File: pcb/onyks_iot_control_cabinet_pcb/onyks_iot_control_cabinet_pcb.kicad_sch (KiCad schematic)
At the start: 20 parts, among them J4 Conn_01x02_Socket, Q3 SQ4940CEY-T1_GE3, SW1 SW_Push, SW2 SW_Push, SW3 SW_Push

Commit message: Fix the project; cleaning up the things
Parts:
- removed BZ?: Buzzer, symbol Device:Buzzer
- removed J4: Conn_01x02_Socket, symbol Connector:Conn_01x02_Socket
- removed Q3, Q?: SQ4940CEY-T1_GE3, symbol Simulation_SPICE:NMOS
- removed Q? (x2): NPN, symbol Simulation_SPICE:NPN
- removed R? (x2): 10k, symbol Device:R
- removed R?: 100, symbol Device:R
- removed U?: ESP32-WROOM-32D, RF_Module:ESP32-WROOM-32D, symbol RF_Module:ESP32-WROOM-32D
- added BZ1: Buzzer, symbol Device:Buzzer
- added J1: Conn_01x02_Socket, symbol Connector:Conn_01x02_Socket
- added Q1, Q2: SQ4940CEY-T1_GE3, symbol Simulation_SPICE:NMOS
- added Q3, Q4: NPN, symbol Simulation_SPICE:NPN
- added R2: 100, symbol Device:R
- added R3, R4: 10k, symbol Device:R
- added U1: ESP32-WROOM-32D, RF_Module:ESP32-WROOM-32D, symbol RF_Module:ESP32-WROOM-32D
- C1: value 0.1u -> 22u
- C4: value 22u -> 0.1u
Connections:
- net +12V: now also BZ1.1 (+)
- net +3.3V: now also C1.1, C2.1, J1.1 (Pin_1), U1.2 (VDD); no longer C3.1, C4.1
- net BUZZER_SWITCH: now also Q2.2 (G), R2.1, U1.26 (IO4)
- net DTR: now also Q3.3 (E), R4.2
- net FREE_GPIO_1: now also U1.24 (IO2)
- net FREE_GPIO_2: now also U1.29 (IO5)
- net FREE_GPIO_3: now also U1.27 (IO16)
- net FREE_GPIO_4: now also U1.28 (IO17)
- net FREE_GPIO_7: now also U1.7 (IO35)
- net GND: now also C1.2, C2.2, C3.1, C4.1, Q1.3 (S), Q2.3 (S), R2.2, U1.1 (GND), U1.15 (GND), U1.38 (GND), U1.39 (GND); no longer C1.1, C2.1, C3.2, C4.2
- net JTAG_MTCK: now also U1.16 (IO13)
- net JTAG_MTDI: now also U1.14 (IO12)
- net JTAG_MTDO: now also U1.23 (IO15)
- net JTAG_MTMS: now also U1.13 (IO14)
- net LOCK_MCU_MANUAL_OPEN: now also J1.2 (Pin_2), U1.31 (IO19)
- net LOCK_MINUS: now also Q1.1 (D)
- net LOCK_SWITCH: now also Q1.2 (G), U1.30 (IO18)
- net MCU_BOOT: now also C3.2, Q3.1 (C), U1.25 (IO0); no longer C1.2
- net MCU_RESET: now also C4.2, Q4.1 (C), U1.3 (EN); no longer C2.2
- net MCU_RX_PROG: now also U1.34 (RXD0/IO3)
- net MCU_TX_PROG: now also U1.35 (TXD0/IO1)
- net NFC_IRQ: now also U1.11 (IO26)
- net NFC_MISO: now also U1.10 (IO25)
- net NFC_MOSI: now also U1.37 (IO23)
- net NFC_RST: now also U1.12 (IO27)
- net RTS: now also Q4.3 (E), R3.2
- net at D1.4 (BK): now also U1.6 (IO34)
- net at D1.2 (RK): now also U1.8 (IO32)
- net at D1.3 (GK): now also U1.9 (IO33)
- new net: Q4.2 (B), R4.1
- new net: BZ1.2 (-), Q2.1 (D)
- new net: Q3.2 (B), R3.1
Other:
- removed sheet Connnectors
- removed sheet Power Supply and NFC Connector
- added sheet connnectors (connectors.kicad_sch)
- added sheet power_supply_nfc_connector (power_supply_nfc_connector.kicad_sch)
- title: Onyks IoT Control Cabinet -> Onyks Iot Control Cabinet

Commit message: Assignment some footprints to symbols
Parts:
- J1: footprint (none) -> Connector_PinHeader_2.54mm:PinHeader_1x02_P2.54mm_Vertical
- Q1, Q2: footprint (none) -> ourFootprints:QFN50P600X600X100-41N-D
- R1, R2, R3, R4: footprint (none) -> Resistor_SMD:R_0805_2012Metric_Pad1.20x1.40mm_HandSolder
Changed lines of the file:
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@@
 			)
 		)
-		(property "Footprint" ""
+		(property "Footprint" "Resistor_SMD:R_0805_2012Metric_Pad1.20x1.40mm_HandSolder"
 			(at 126.492 176.53 90)
 			(effects
@@
 			)
 		)
-		(property "Footprint" ""
+		(property "Footprint" "Resistor_SMD:R_0805_2012Metric_Pad1.20x1.40mm_HandSolder"
 			(at 138.43 56.388 90)
 			(effects
@@
 			)
 		)
-		(property "Footprint" ""
+		(property "Footprint" "ourFootprints:QFN50P600X600X100-41N-D"
 			(at 67.31 170.18 0)
 			(effects
@@
 			)
 		)
-		(property "Footprint" ""
+		(property "Footprint" "Resistor_SMD:R_0805_2012Metric_Pad1.20x1.40mm_HandSolder"
 			(at 138.43 76.708 90)
 			(effects
@@
 			)
 		)
-		(property "Footprint" ""
+		(property "Footprint" "Resistor_SMD:R_0805_2012Metric_Pad1.20x1.40mm_HandSolder"
 			(at 49.022 176.53 90)
 			(effects
@@
 			)
 		)
-		(property "Footprint" ""
+		(property "Footprint" "ourFootprints:QFN50P600X600X100-41N-D"
 			(at 144.78 170.18 0)
 			(effects
@@
 			)
 		)
-		(property "Footprint" ""
+		(property "Footprint" "Connector_PinHeader_2.54mm:PinHeader_1x02_P2.54mm_Vertical"
 			(at 237.49 72.39 0)
 			(effects

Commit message: PCB - Finished, needs additional confirmation
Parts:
- removed D1: LED_ARGB, symbol Device:LED_ARGB
- added D1: WS2812B, LED_SMD:LED_WS2812B_PLCC4_5.0x5.0mm_P3.2mm, symbol LED:WS2812B
- BZ1: footprint (none) -> ourFootprints:CPI2416100T
- C1, C2, C3, C4, C5: footprint (none) -> Capacitor_SMD:C_0805_2012Metric
- Q1, Q2: footprint ourFootprints:QFN50P600X600X100-41N-D -> ourFootprints:SOIC127P600X175-8N
- Q3, Q4: footprint (none) -> Package_TO_SOT_SMD:SOT-23-3
- SW1, SW2, SW3: footprint (none) -> Button_Switch_SMD:SW_Push_SPST_NO_Alps_SKRK
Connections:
- net +12V: now also BZ1.A1 (-_1), BZ1.B1 (+_1), BZ1.B2 (+_2); no longer BZ1.1 (+)
- net +3.3V: now also D1.1 (VDD)
- net BUZZER_SWITCH: now also Q2.4 (G); no longer Q2.2 (G)
- net FREE_GPIO_5: now also U1.33 (IO21)
- net FREE_GPIO_6: now also U1.36 (IO22)
- net FREE_GPIO_7: now also U1.9 (IO33); no longer U1.7 (IO35)
- net GND: now also Q1.1 (S), Q1.2 (S), Q2.1 (S), Q2.2 (S), D1.3 (VSS)
- net LOCK_MINUS: now also Q1.5 (D), Q1.6 (D), Q1.7 (D), Q1.8 (D); no longer Q1.1 (D)
- net LOCK_SWITCH: now also Q1.4 (G); no longer Q1.2 (G)
- net FREE_GPIO_8: now reaches U1.6 (IO34)
- net at U1.8 (IO32): now also D1.4 (DIN)
- new net: BZ1.A2 (-_2), Q2.5 (D), Q2.6 (D), Q2.7 (D), Q2.8 (D)
- new net FREE_GPIO_9: U1.7 (IO35)
- no-connect marks 8 -> 9
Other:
- sheet connnectors ports: added GPIO_8, GPIO_9; removed none

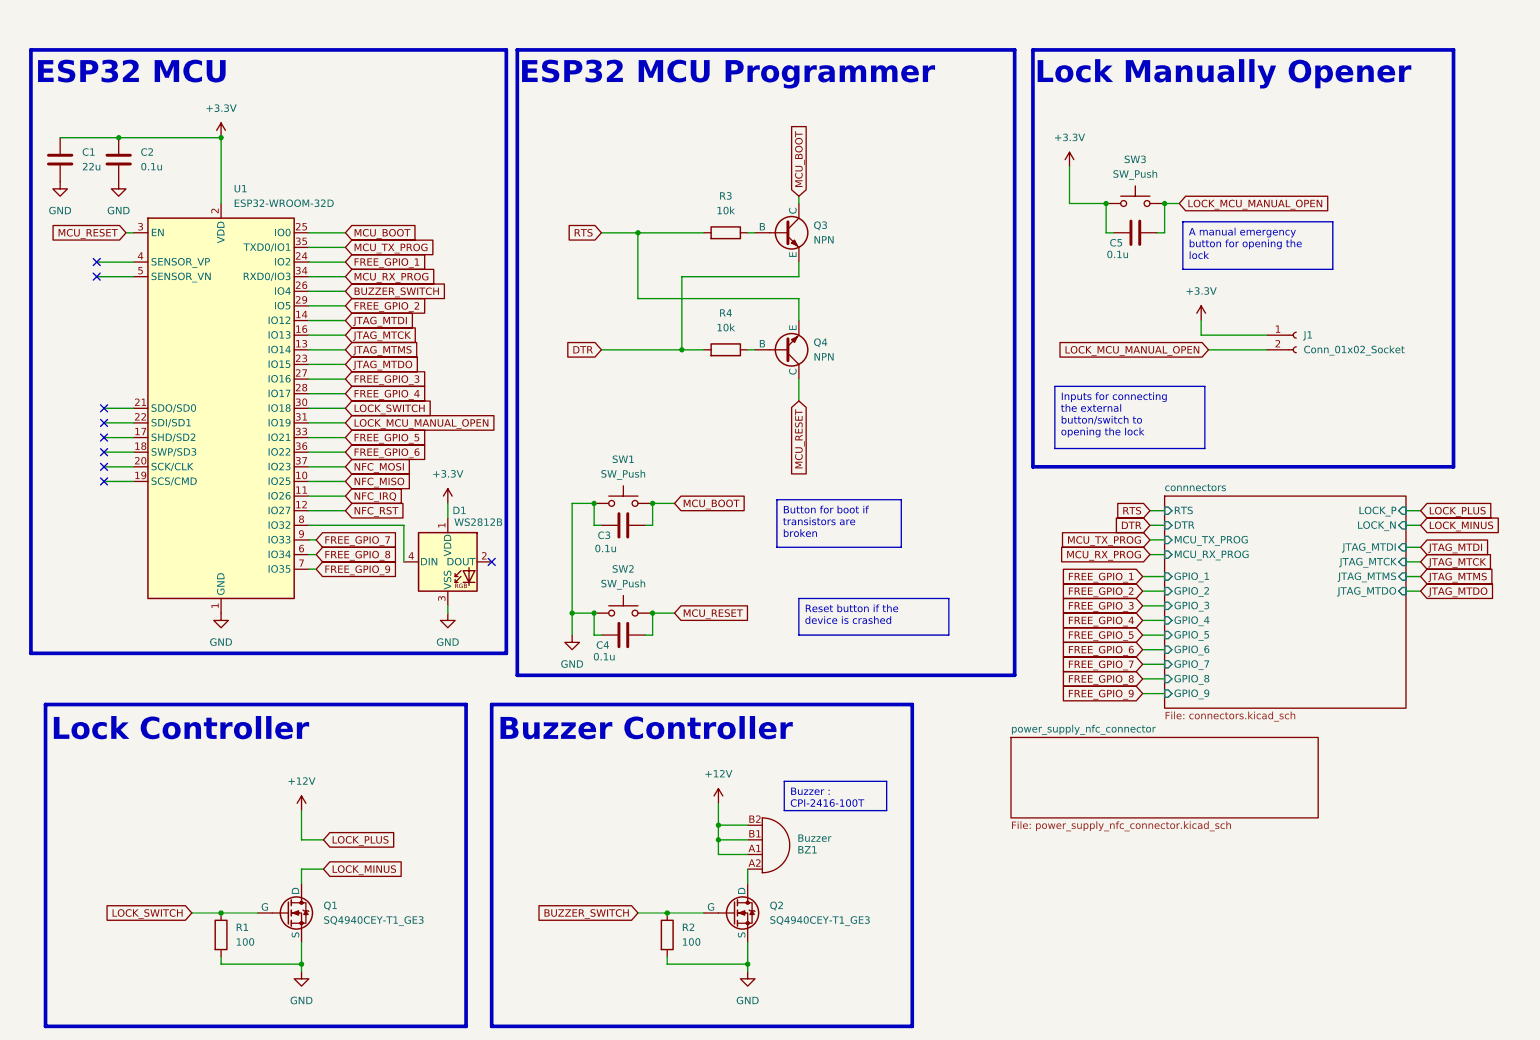
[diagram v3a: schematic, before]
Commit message: Change some elements footprints
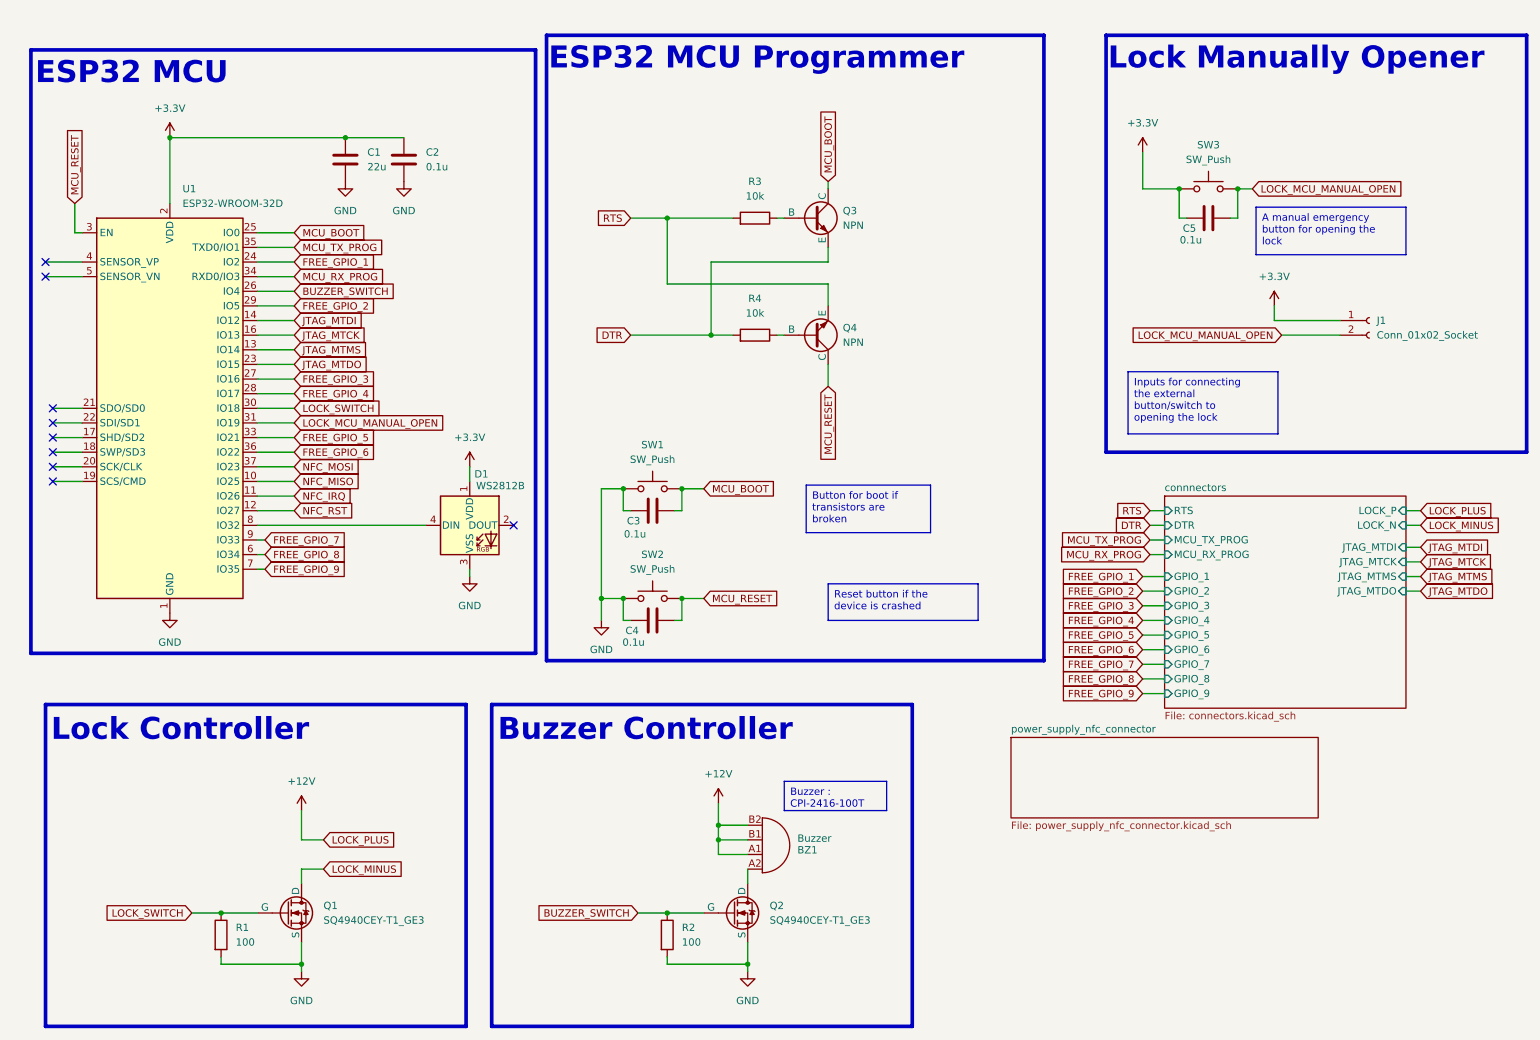
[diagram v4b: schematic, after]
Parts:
- SW1, SW2, SW3: footprint Button_Switch_SMD:SW_Push_SPST_NO_Alps_SKRK -> Button_Switch_SMD:SW_Tactile_SPST_NO_Straight_CK_PTS636Sx25SMTRLFS
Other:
- moved on the sheet: C1, C2, C3, C4, C5, D1, J1, Q3, Q4, R3, R4, SW1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

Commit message: Fixed minor mistakes (name of MOS component)
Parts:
- Q1, Q2: value SQ4940CEY-T1_GE3 -> SQ4050EY-T1_GE3
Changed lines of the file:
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@@
 			)
 		)
-		(property "Value" "SQ4940CEY-T1_GE3"
+		(property "Value" "SQ4050EY-T1_GE3"
 			(at 146.05 173.9899 0)
 			(effects
@@
 			)
 		)
-		(property "Value" "SQ4940CEY-T1_GE3"
+		(property "Value" "SQ4050EY-T1_GE3"
 			(at 68.58 173.9899 0)
 			(effects

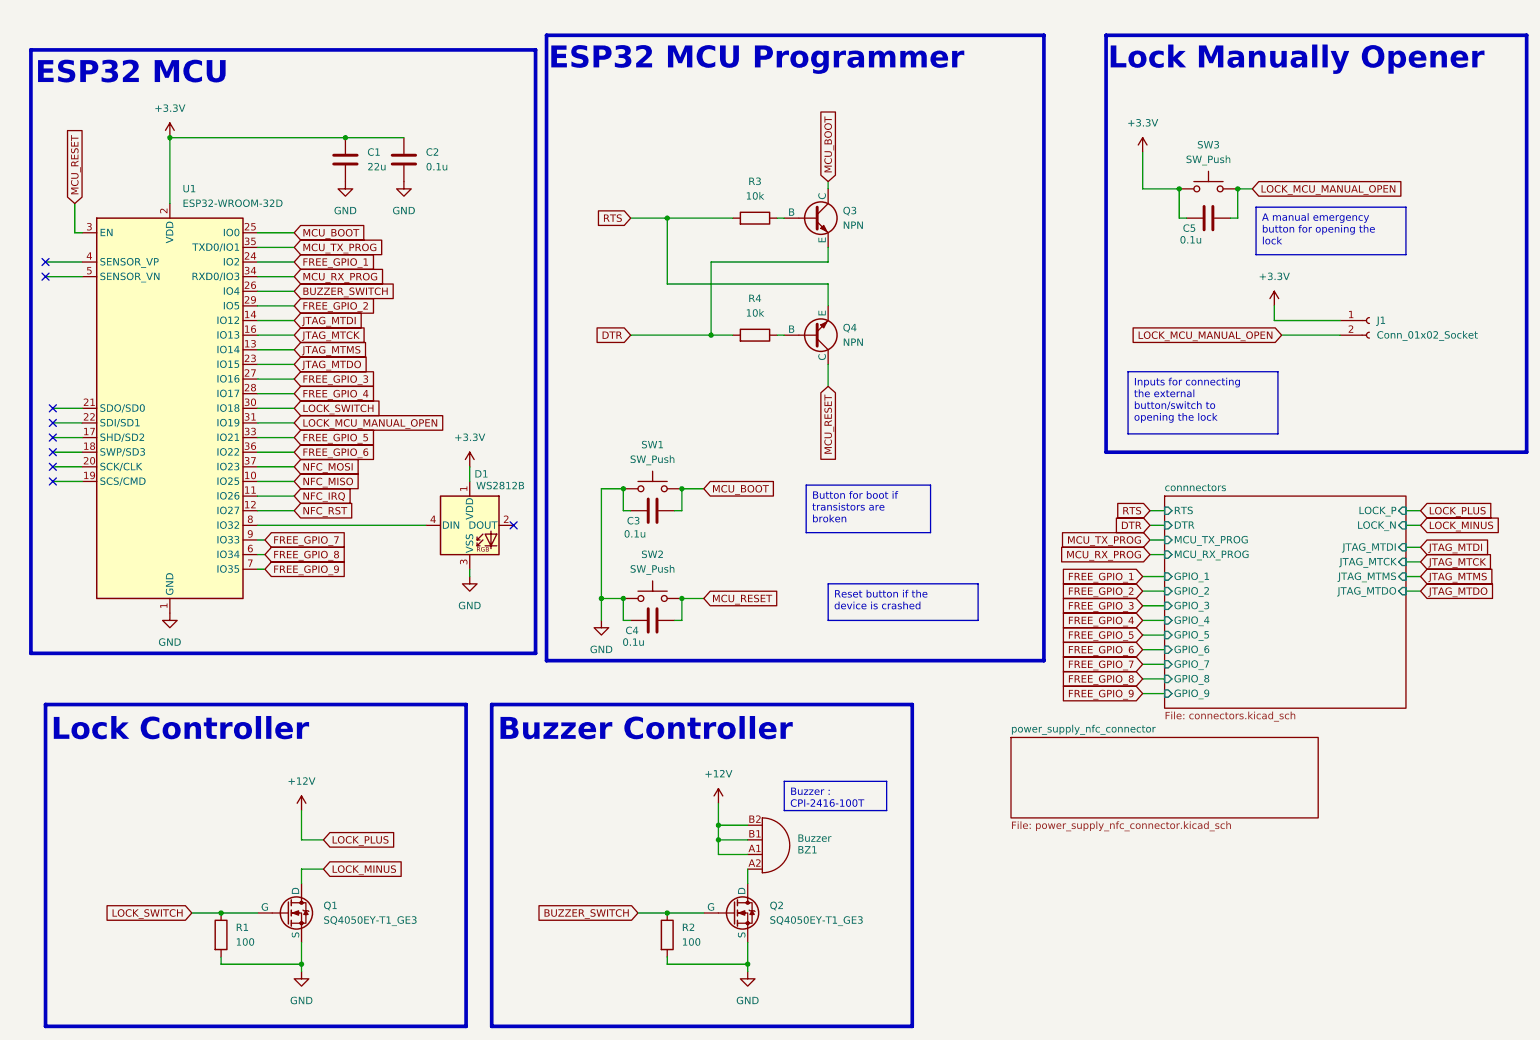
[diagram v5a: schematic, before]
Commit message: Redrawing schematics
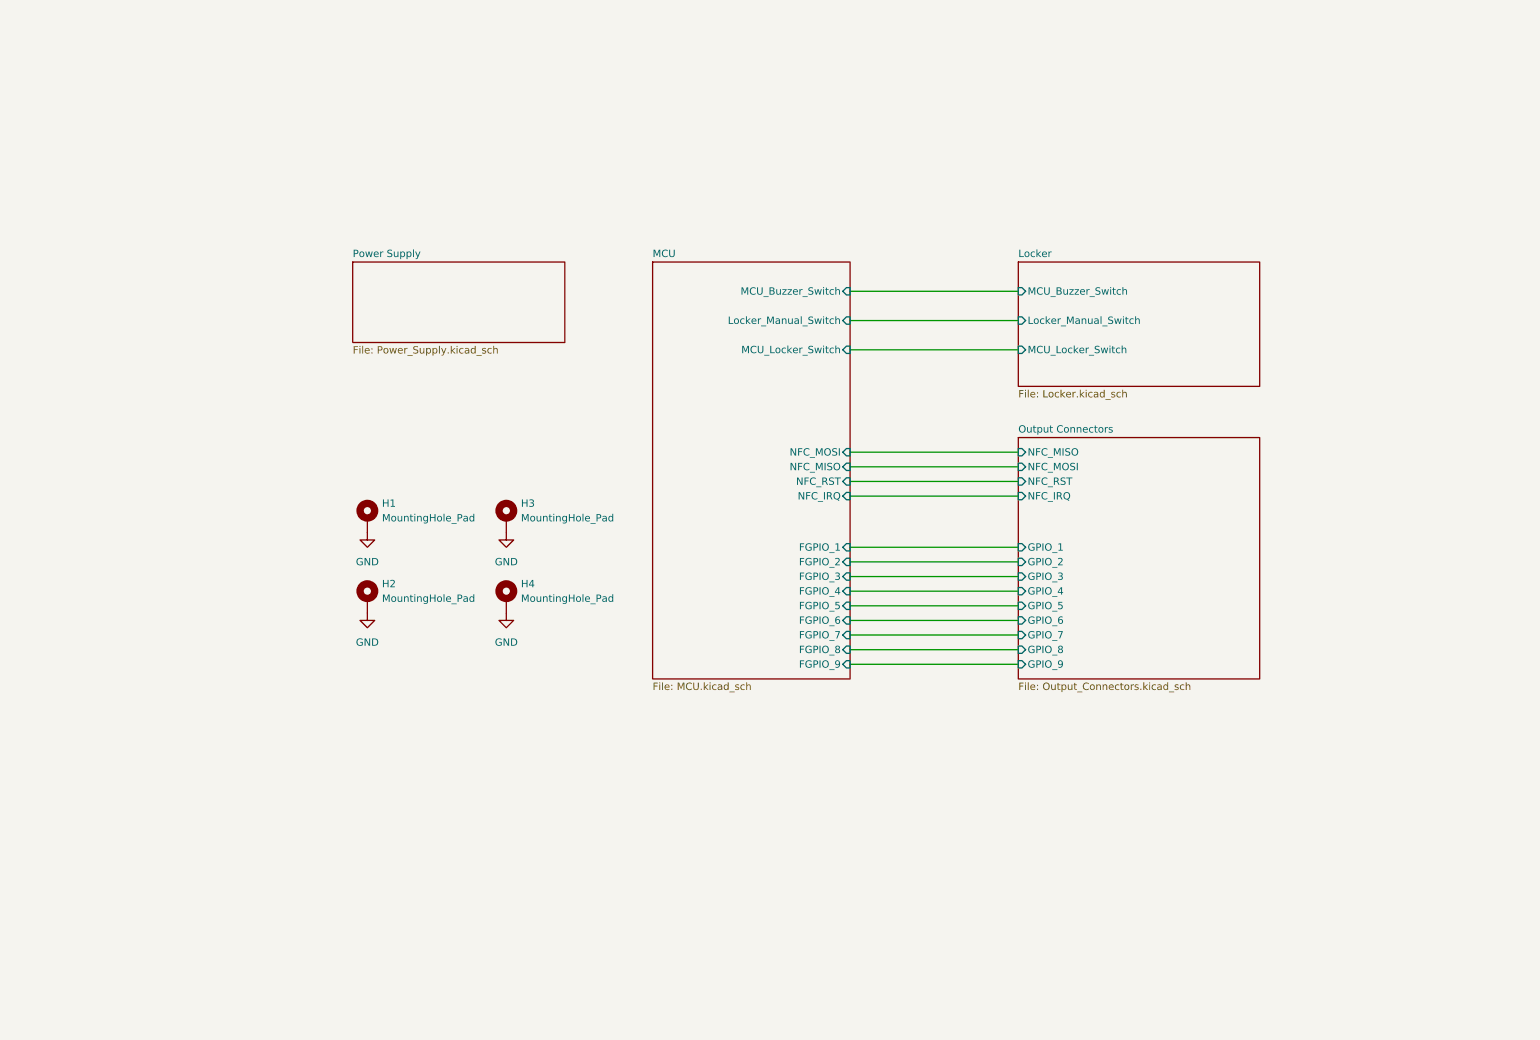
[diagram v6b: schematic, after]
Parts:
- removed BZ1: Buzzer, ourFootprints:CPI2416100T, symbol Device:Buzzer
- removed C1: 22u, Capacitor_SMD:C_0805_2012Metric, symbol Device:C
- removed C2, C3, C4, C5: 0.1u, Capacitor_SMD:C_0805_2012Metric, symbol Device:C
- removed D1: WS2812B, LED_SMD:LED_WS2812B_PLCC4_5.0x5.0mm_P3.2mm, symbol LED:WS2812B
- removed J1: Conn_01x02_Socket, Connector_PinHeader_2.54mm:PinHeader_1x02_P2.54mm_Vertical, symbol Connector:Conn_01x02_Socket
- removed Q1, Q2: SQ4050EY-T1_GE3, ourFootprints:SOIC127P600X175-8N, symbol Simulation_SPICE:NMOS
- removed Q3, Q4: NPN, Package_TO_SOT_SMD:SOT-23-3, symbol Simulation_SPICE:NPN
- removed R1, R2: 100, Resistor_SMD:R_0805_2012Metric_Pad1.20x1.40mm_HandSolder, symbol Device:R
- removed R3, R4: 10k, Resistor_SMD:R_0805_2012Metric_Pad1.20x1.40mm_HandSolder, symbol Device:R
- removed SW1, SW2, SW3: SW_Push, Button_Switch_SMD:SW_Tactile_SPST_NO_Straight_CK_PTS636Sx25SMTRLFS, symbol Switch:SW_Push
- removed U1: ESP32-WROOM-32D, RF_Module:ESP32-WROOM-32D, symbol RF_Module:ESP32-WROOM-32D
- added H1, H2, H3, H4: MountingHole_Pad, MountingHole:MountingHole_3.2mm_M3_DIN965_Pad_TopBottom, symbol Mechanical:MountingHole_Pad
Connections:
- net GND: now also H1.1, H2.1, H3.1, H4.1
- no-connect marks 9 -> 0
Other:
- sheet connnectors renamed Output Connectors
- sheet power_supply_nfc_connector renamed Power Supply
- added sheet Locker (Locker.kicad_sch)
- added sheet MCU (MCU.kicad_sch)
- sheet Output Connectors: file connectors.kicad_sch -> Output_Connectors.kicad_sch
- sheet Output Connectors ports: added NFC_IRQ, NFC_MISO, NFC_MOSI, NFC_RST; removed DTR, JTAG_MTCK, JTAG_MTDI, JTAG_MTDO, JTAG_MTMS, LOCK_N, LOCK_P, MCU_RX_PROG, MCU_TX_PROG, RTS
- sheet Power Supply: file power_supply_nfc_connector.kicad_sch -> Power_Supply.kicad_sch
- note removed: "Buzzer Controller"
- note removed: "ESP32 MCU"
- note removed: "ESP32 MCU Programmer"
- note removed: "Lock Controller"
- note removed: "Lock Manually Opener"

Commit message: Quick Fixes
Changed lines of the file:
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@@
+	(wire
+		(pts
+			(xy 160.02 92.71) (xy 189.23 92.71)
+		)
+		(stroke
+			(width 0)
+			(type default)
+		)
+	)
 	(wire
 		(pts
@@
 	(wire
 		(pts
+			(xy 160.02 64.77) (xy 189.23 64.77)
+		)
+		(stroke
+			(width 0)
+			(type default)
+		)
+	)
+	(wire
+		(pts
 			(xy 160.02 95.25) (xy 189.23 95.25)
 		)
@@
 	(wire
 		(pts
-			(xy 160.02 64.77) (xy 189.23 64.77)
-		)
-		(stroke
-			(width 0)
-			(type default)
-		)
-	)
-	(wire
-		(pts
 			(xy 160.02 109.22) (xy 189.23 109.22)
 		)
@@
 		(pts
 			(xy 160.02 119.38) (xy 189.23 119.38)
-		)
-		(stroke
-			(width 0)
-			(type default)
-		)
-	)
-	(wire
-		(pts
-			(xy 160.02 92.71) (xy 189.23 92.71)
 		)
 		(stroke
@@
 		)
 		(pin "NFC_MISO" input
+			(at 189.23 95.25 180)
+			(effects
+				(font
+					(size 1.27 1.27)
+				)
+				(justify left)
+			)
+		)
+		(pin "NFC_MOSI" input
 			(at 189.23 92.71 180)
 			(effects
 				(font
-					(size 1.27 1.27)
-				)
-				(justify left)
-			)
-		)
-		(pin "NFC_MOSI" input
-			(at 189.23 95.25 180)
-			(effects
-				(font
